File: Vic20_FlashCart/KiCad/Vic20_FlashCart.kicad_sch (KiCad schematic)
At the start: 45 parts, among them J3 Pin Headers, U1 SST39LF040, U2 SST39LF040, U3 IS62C256AL, U4 SN74HCT00PWR, U5 CD74HCT21M96, X1 Cart Fingers

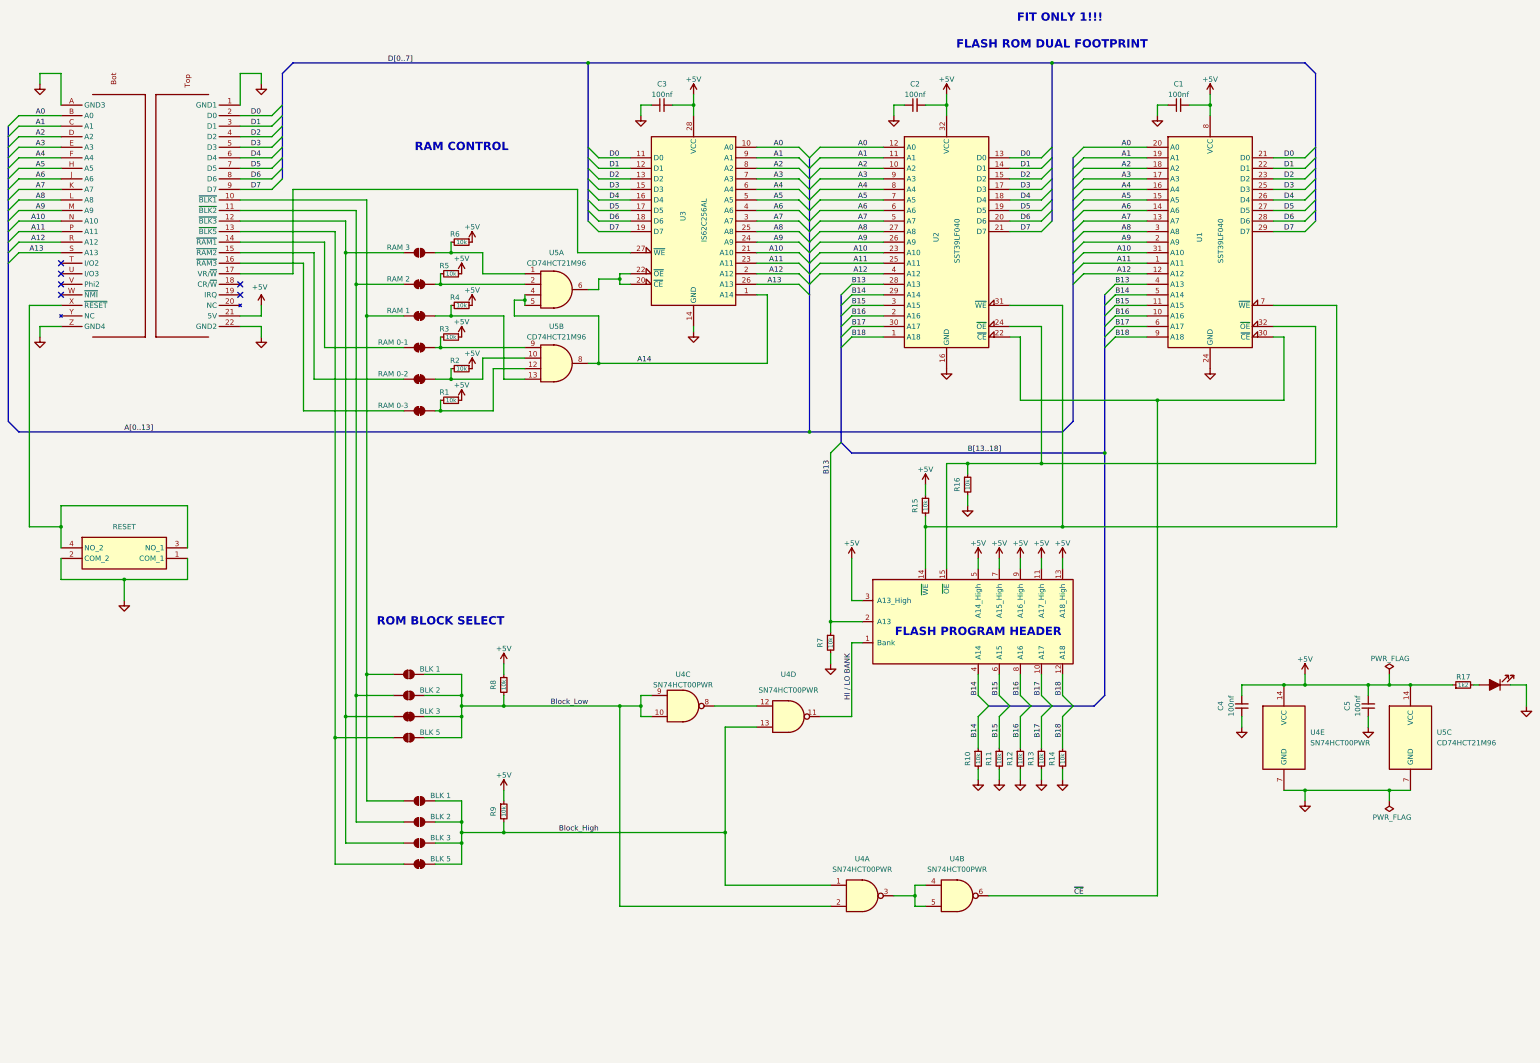
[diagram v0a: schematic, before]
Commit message: - Updated To KiCad 10.0
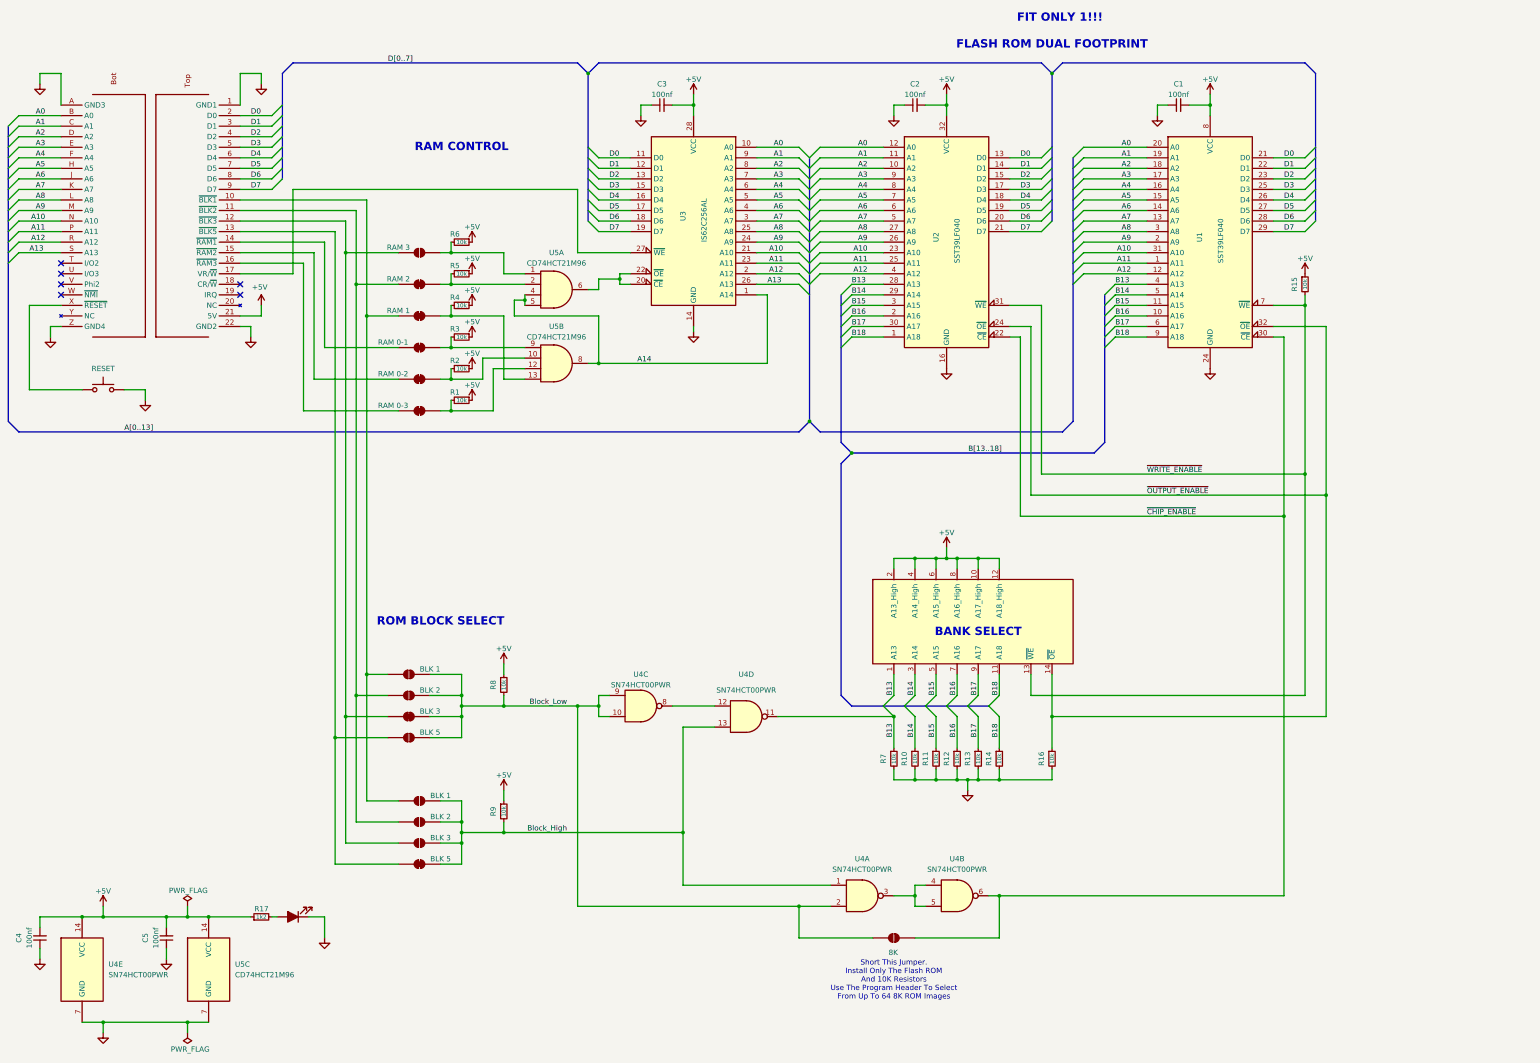
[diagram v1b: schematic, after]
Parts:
- added JP16: 8K, Jumper:SolderJumper-2_P1.3mm_Open_RoundedPad1.0x1.5mm, symbol Jumper:SolderJumper_2_Open
- J3: footprint Dave Footprints:PinHeader_Vic20_Cartridge -> _Custom:PinHeader_Vic20_Cartridge; symbol Dave:Conn_Vic20_Cartridge -> _Custom:Header_Banks_Vic20_Cart
- S1: footprint SamacSys_Parts:B3F1052G -> Button_Switch_THT:SW_PUSH_6mm_H4.3mm; symbol SamacSys_Parts:B3F-1052-G -> Switch:SW_Push
- U5: symbol 74xx:74LS21 -> _Custom:74LS21
- X1: footprint Dave Footprints:VIC20-Cart-Num -> _Custom:VIC20-Cart-Num; symbol Dave:VIC20_CARTRIDGE -> _Custom:VIC20_CARTRIDGE
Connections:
- net HI / LO BANK is gone; now on net B13: J3.1 (A13), U4.11
- net +5V: now also J3.10 (A17_High), J3.12 (A18_High), J3.2 (A13_High), J3.4 (A14_High), J3.6 (A15_High), J3.8 (A16_High); no longer J3.11 (A17_High), J3.13 (A18_High), J3.3 (A13_High), J3.5 (A14_High), J3.7 (A15_High), J3.9 (A16_High)
- net B13: no longer J3.2 (A13)
- net B14: now also J3.3 (A14); no longer J3.4 (A14)
- net B15: now also J3.5 (A15); no longer J3.6 (A15)
- net B16: now also J3.7 (A16); no longer J3.8 (A16)
- net B17: now also J3.9 (A17); no longer J3.10 (A17)
- net B18: now also J3.11 (A18); no longer J3.12 (A18)
- net Block_Low: now also JP16.1 (A)
- net GND: no longer S1.1 (COM_1)
- net ~{OUTPUT_ENABLE}: now reaches R16.1, U1.32 (~{OE}), U2.24 (~{OE})
- net ~{OUTPUT_ENABLE}: now also J3.14 (~{OE}); no longer J3.15 (~{OE})
- net ~{WRITE_ENABLE}: now reaches R15.2, U1.7 (~{WE}), U2.31 (~{WE})
- net ~{WRITE_ENABLE}: now also J3.13 (~{WE}); no longer J3.14 (~{WE})
- net ~{CE} renamed ~{CHIP_ENABLE}
- net ~{CHIP_ENABLE}: now also JP16.2 (B)
- new net: S1.1, X1.X (~{RESET})
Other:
- note added: "BANK SELECT"
- note added: "Short This Jumper. Install Only The Flash ROM And 10K Resistors Use The Program Header To Select From Up To 64 8K ROM Images"
- note removed: "FLASH PROGRAM HEADER"
- moved on the sheet: C4, C5, R1, R10, R11, R12, R13, R14, R17, R3, R5, U4C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
